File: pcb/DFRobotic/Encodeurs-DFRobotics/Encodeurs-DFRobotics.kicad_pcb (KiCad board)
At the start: 2 copper layers, 47 x 20 mm, 12 parts, among them J1 DF3A-5P-2DS, J2 DF3A-5P-2DS, U1 AEDR-8300, U2 AEDR-8300, U3 74LVC2G34, U4 74LVC2G34

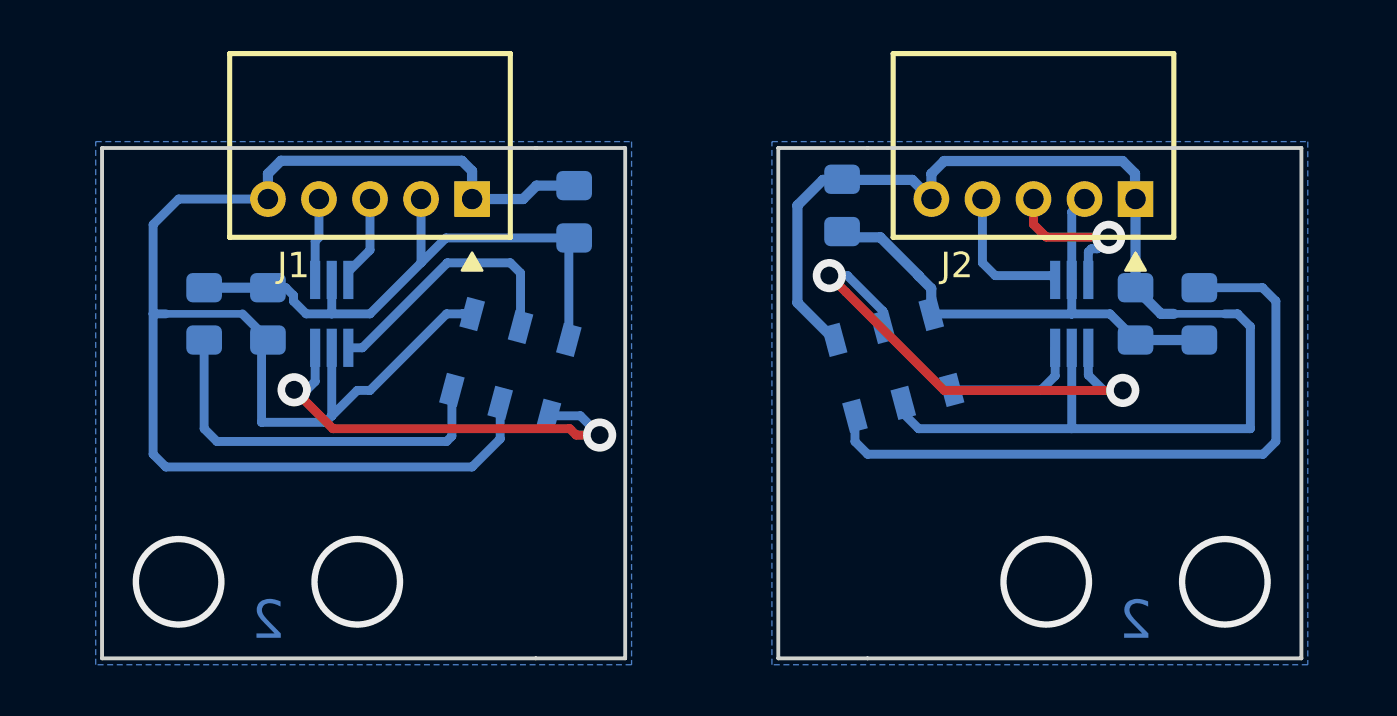
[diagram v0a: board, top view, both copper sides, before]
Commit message: Ajout des regles NXP Cup pour 2020 (V1) + modifs mineures sur pcbs
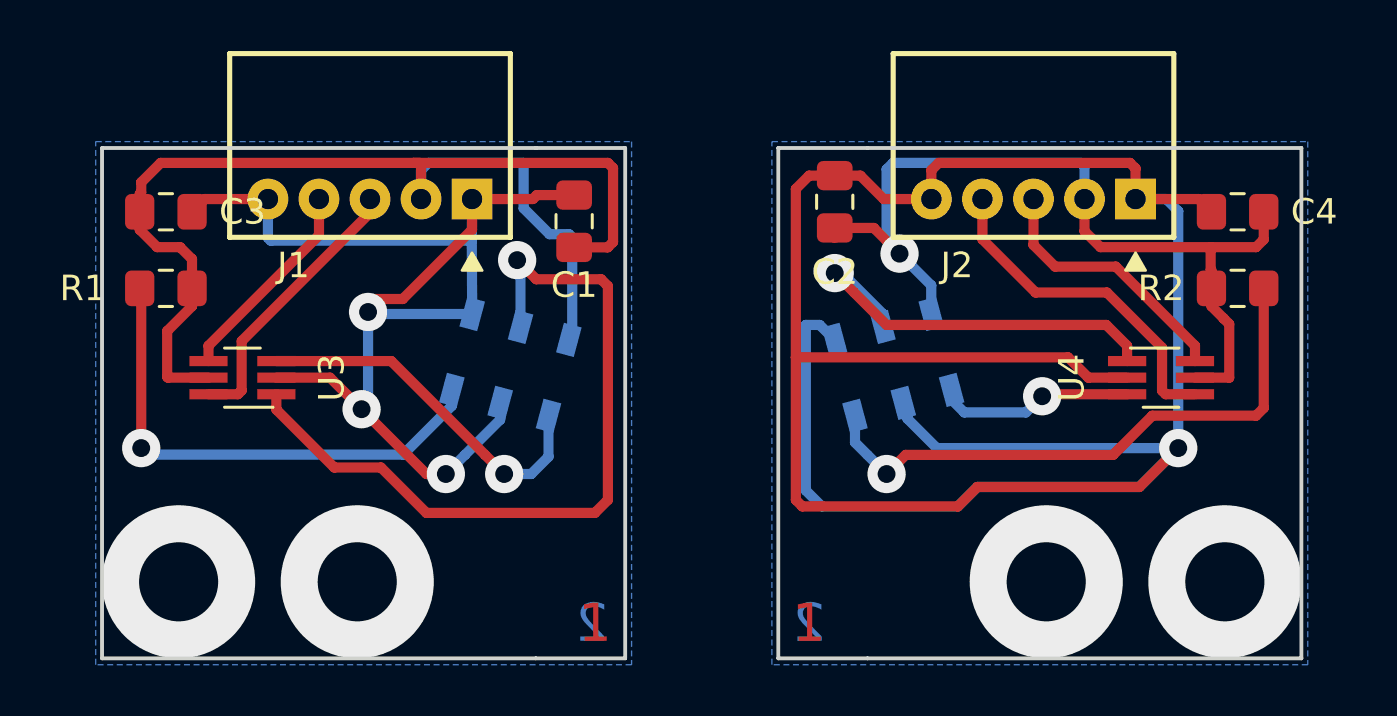
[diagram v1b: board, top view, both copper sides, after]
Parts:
- C1, C2, C3, C4, R1, R2, U3, U4: moved to F.Cu
- moved C3 5.66 mm to (82.5, 102.5), turned to 0 degrees
- moved C4 5.66 mm to (124.5, 102.5), turned to 180 degrees
- moved U3 4.30 mm to (85.5, 109.0), turned to 180 degrees
- moved U4 4.30 mm to (121.5, 109.0), turned to 0 degrees
- moved R1 1.80 mm to (82.5, 105.5), turned to 180 degrees
- moved R2 1.80 mm to (124.5, 105.5), turned to 0 degrees
- moved C1 0.37 mm to (98.5, 102.9)
- moved C2 0.32 mm to (108.7, 102.1)
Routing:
- net +5V: track 45.2 -> 84.9 mm, vias 0 -> 1
- net GND: track 117.5 -> 155.9 mm, vias 0 -> 4
- net Net-(U1-Pad5): track 10.4 -> 30.5 mm, vias 0 -> 1
- net /SENS_RIGHT_B: track 5.64 -> 13.4 mm
- net /SENS_LEFT_A: track 3.52 -> 10.9 mm
- net /SENS_LEFT_B: track 3.23 -> 8.14 mm
- net Net-(R1-Pad2): track 15.3 -> 20.0 mm, vias 0 -> 1
- net /SENS_RIGHT_A: track 6.29 -> 10.4 mm, vias 1 -> 0
- net Net-(R2-Pad2): track 26.6 -> 23.3 mm, vias 0 -> 1
- net Net-(U2-Pad5): track 19.3 -> 16.3 mm, vias 2 -> 1
- net Net-(U1-Pad1): track 17.3 -> 14.4 mm, vias 2 -> 1
- net Net-(U2-Pad1): track 5.39 -> 7.76 mm, vias 0 -> 1
- added copper zone on F.Cu, net GND
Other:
- board text added: "1"

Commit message: Changement de capteur pour les encodeurs DFRobot
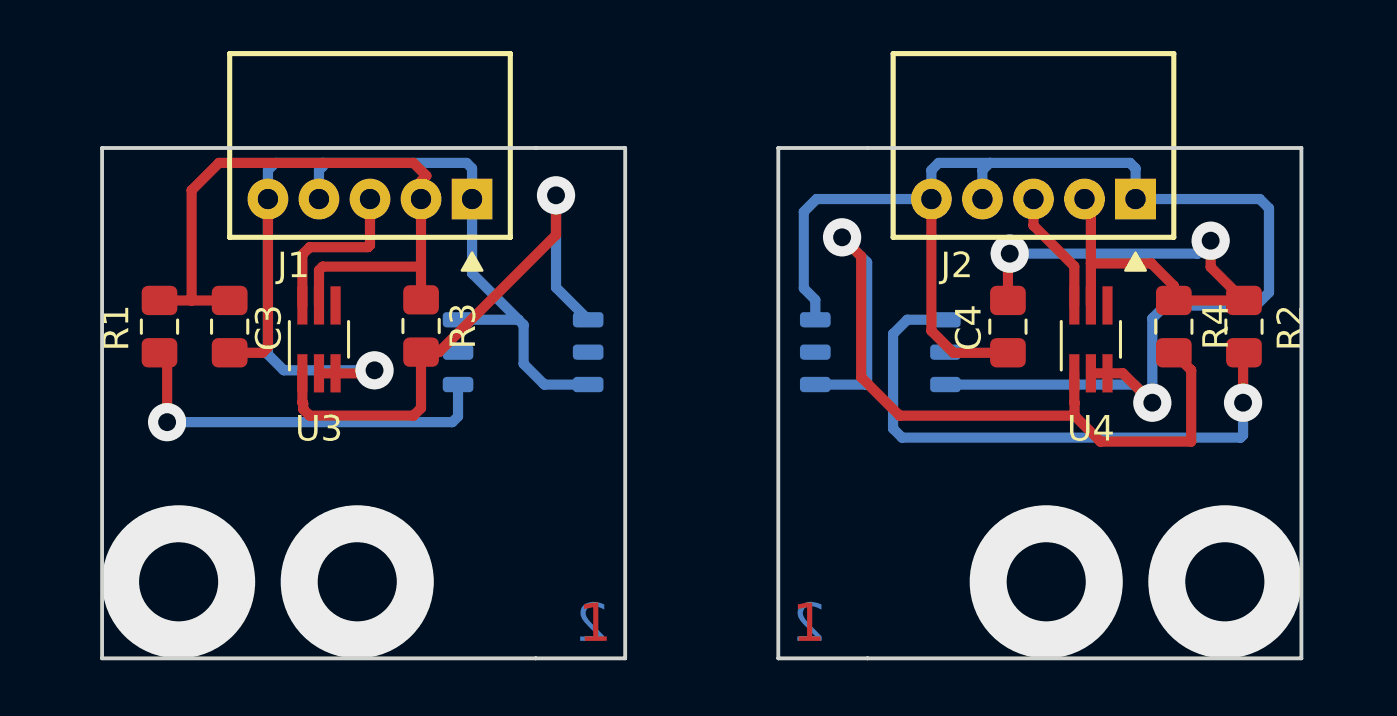
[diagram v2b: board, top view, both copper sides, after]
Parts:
- removed C1, C2: 1µF, Capacitor_SMD:C_0805_2012Metric_Pad1.15x1.40mm_HandSolder
- added R3: 200, Resistor_SMD:R_0805_2012Metric_Pad1.15x1.40mm_HandSolder, F.Cu at (92.5, 107.0)
- added R4: 200, Resistor_SMD:R_0805_2012Metric_Pad1.15x1.40mm_HandSolder, F.Cu at (122.0, 107.0)
- U1, U2: value AEDR-8300 -> SFH9206; footprint Insa:AEDR-8300 -> OptoDevice:Osram_SFH9x0x
- moved C4 10.1 mm to (115.5, 107.0), turned to 270 degrees
- moved C3 5.15 mm to (85.0, 107.0), turned to 270 degrees
- moved U3 3.35 mm to (88.5, 107.5), turned to 90 degrees
- moved U4 3.13 mm to (118.8, 107.5), turned to 90 degrees
- moved R1 1.52 mm to (82.2, 107.0), turned to 90 degrees
- moved R2 1.52 mm to (124.8, 107.0), turned to 90 degrees
- moved U1 0.71 mm to (96.5, 108.0), turned to 0 degrees
- moved U2 0.71 mm to (110.5, 108.0), turned to 180 degrees
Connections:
- J1 pad 4: /SENS_LEFT_B -> GND
- J2 pad 4: /SENS_RIGHT_B -> GND
- R1 pad 1: +5V -> Net-(R1-Pad1)
- R1 pad 2: Net-(R1-Pad2) -> +5V
- R2 pad 1: +5V -> Net-(R2-Pad1)
- R2 pad 2: Net-(R2-Pad2) -> +5V
- U1 pad 1: Net-(U1-Pad1) -> Net-(R1-Pad1)
- U1 pad 2: GND -> (no net)
- U1 pad 3: Net-(R1-Pad2) -> GND
- U1 pad 4: GND -> Net-(R3-Pad2)
- U1 pad 5: Net-(U1-Pad5) -> (no net)
- U1 pad 6: +5V -> GND
- U2 pad 1: Net-(U2-Pad1) -> Net-(R2-Pad1)
- U2 pad 2: GND -> (no net)
- U2 pad 3: Net-(R2-Pad2) -> GND
- U2 pad 4: GND -> Net-(R4-Pad2)
- U2 pad 5: Net-(U2-Pad5) -> (no net)
- U2 pad 6: +5V -> GND
- U3 pad 1: Net-(U1-Pad5) -> Net-(R3-Pad2)
- U3 pad 3: Net-(U1-Pad1) -> GND
- U3 pad 4: /SENS_LEFT_B -> (no net)
- U4 pad 1: Net-(U2-Pad5) -> Net-(R4-Pad2)
- U4 pad 3: Net-(U2-Pad1) -> GND
- U4 pad 4: /SENS_RIGHT_B -> (no net)
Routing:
- net GND: track 155.9 -> 103.5 mm, vias 4 -> 2
- net +5V: track 84.9 -> 51.3 mm, vias 1 -> 2
- net Net-(R4-Pad2): track 0.00 -> 33.4 mm, vias 0 -> 1
- net Net-(U1-Pad5): track 30.5 -> 0.00 mm, vias 1 -> 0
- net Net-(R2-Pad2): track 23.3 -> 0.00 mm, vias 1 -> 0
- net Net-(R2-Pad1): track 0.00 -> 23.1 mm, vias 0 -> 1
- net Net-(R3-Pad2): track 0.00 -> 22.6 mm, vias 0 -> 1
- net Net-(R1-Pad2): track 20.0 -> 0.00 mm, vias 1 -> 0
- net Net-(U2-Pad5): track 16.3 -> 0.00 mm, vias 1 -> 0
- net Net-(R1-Pad1): track 0.00 -> 15.6 mm, vias 0 -> 1
- net Net-(U1-Pad1): track 14.4 -> 0.00 mm, vias 1 -> 0
- net /SENS_RIGHT_B: track 13.4 -> 0.00 mm
- net /SENS_LEFT_B: track 8.14 -> 0.00 mm
- net Net-(U2-Pad1): track 7.76 -> 0.00 mm, vias 1 -> 0
- net /SENS_RIGHT_A: track 10.4 -> 4.83 mm
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- removed copper zone on B.Cu, net GND
- removed copper zone on F.Cu, net GND
